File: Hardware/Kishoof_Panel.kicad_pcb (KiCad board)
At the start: 2 copper layers, 71 x 128.5 mm, 25 parts

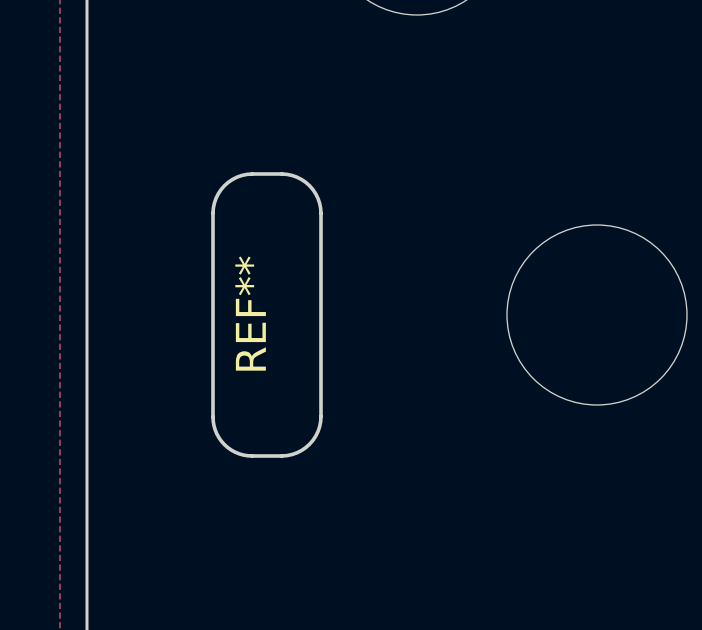
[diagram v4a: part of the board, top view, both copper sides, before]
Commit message: PCBs v1.0 ordered
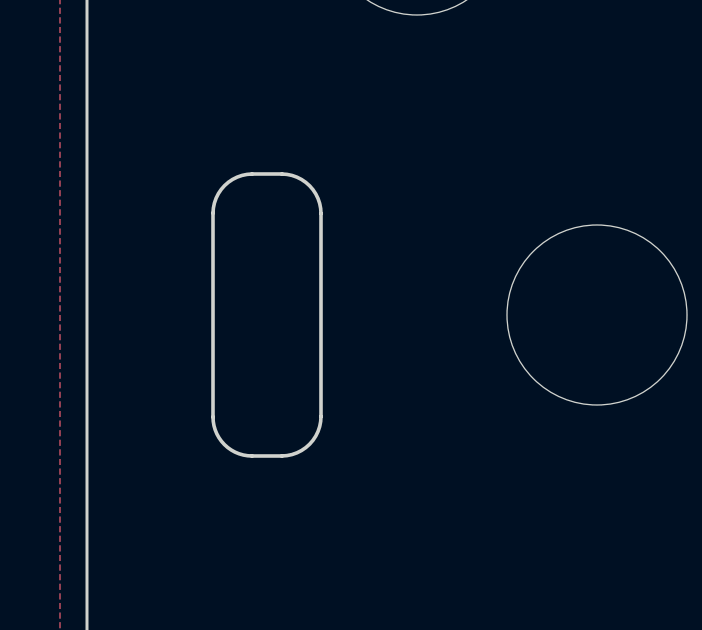
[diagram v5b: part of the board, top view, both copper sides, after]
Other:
- board text added: "Mountjoy Modular 2024 Kishoof Panel v1.0"
- board text removed: "Mountjoy Modular 2024 Kishoof Panel v2.0"
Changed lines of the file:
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@@
 			(drillshape 0)
 			(scaleselection 1)
-			(outputdirectory "Gerbers/Quango_Panel/")
+			(outputdirectory "Gerbers/Kishoof_Panel/")
 		)
 	)
@@
 			(unlocked yes)
 			(layer "F.SilkS")
+			(hide yes)
 			(effects
 				(font
@@
 		)
 	)
-	(gr_text "Mountjoy Modular 2024\nKishoof Panel v2.0"
+	(gr_text "Mountjoy Modular 2024\nKishoof Panel v1.0"
 		(at 90.5 34.85 0)
 		(layer "B.SilkS")

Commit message: More code clean up
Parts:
- added REF**: 3D_Dummy, Custom_Footprints:3D_Dummy, F.Cu at (77.0, 59.0)
- turned Ref** to 90 degrees
